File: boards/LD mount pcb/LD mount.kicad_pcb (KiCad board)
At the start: 2 copper layers, 11 x 11 mm, 5 parts

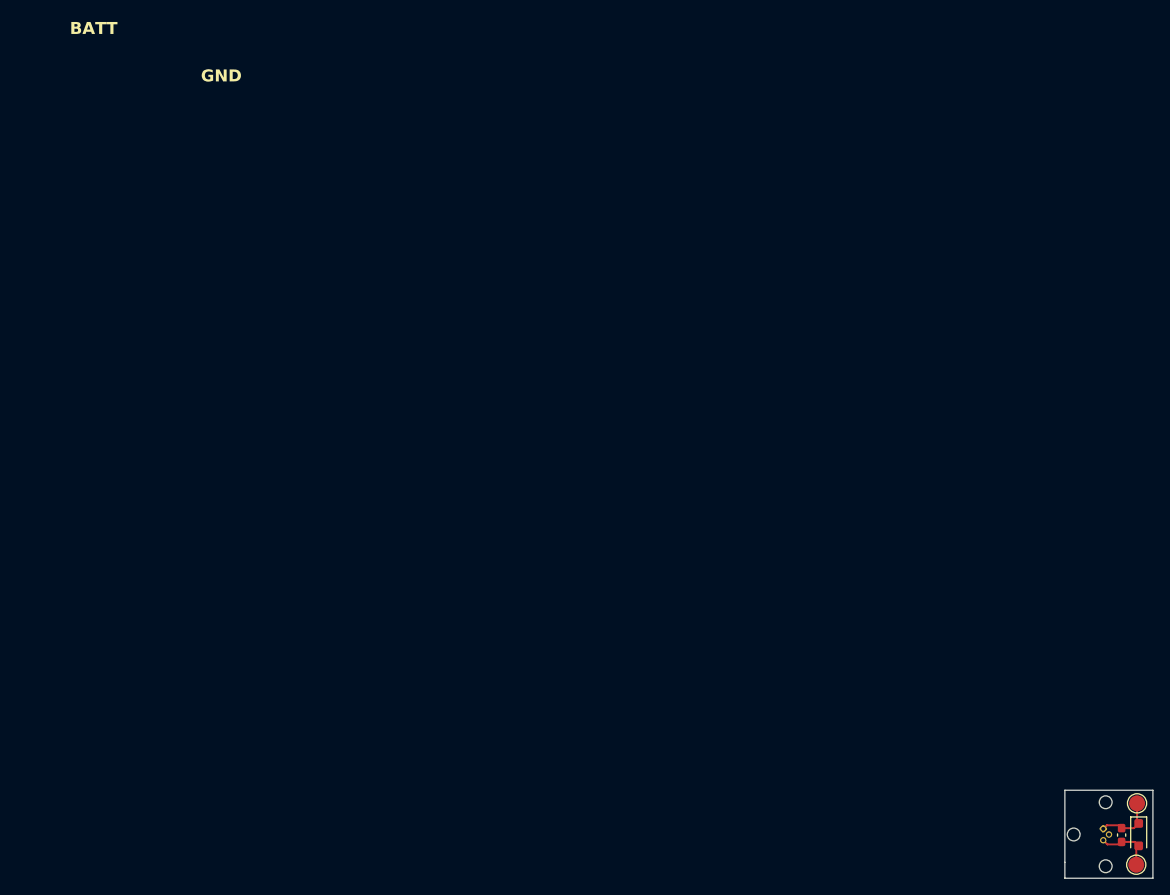
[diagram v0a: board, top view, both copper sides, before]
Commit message: updated physical scanning chassis
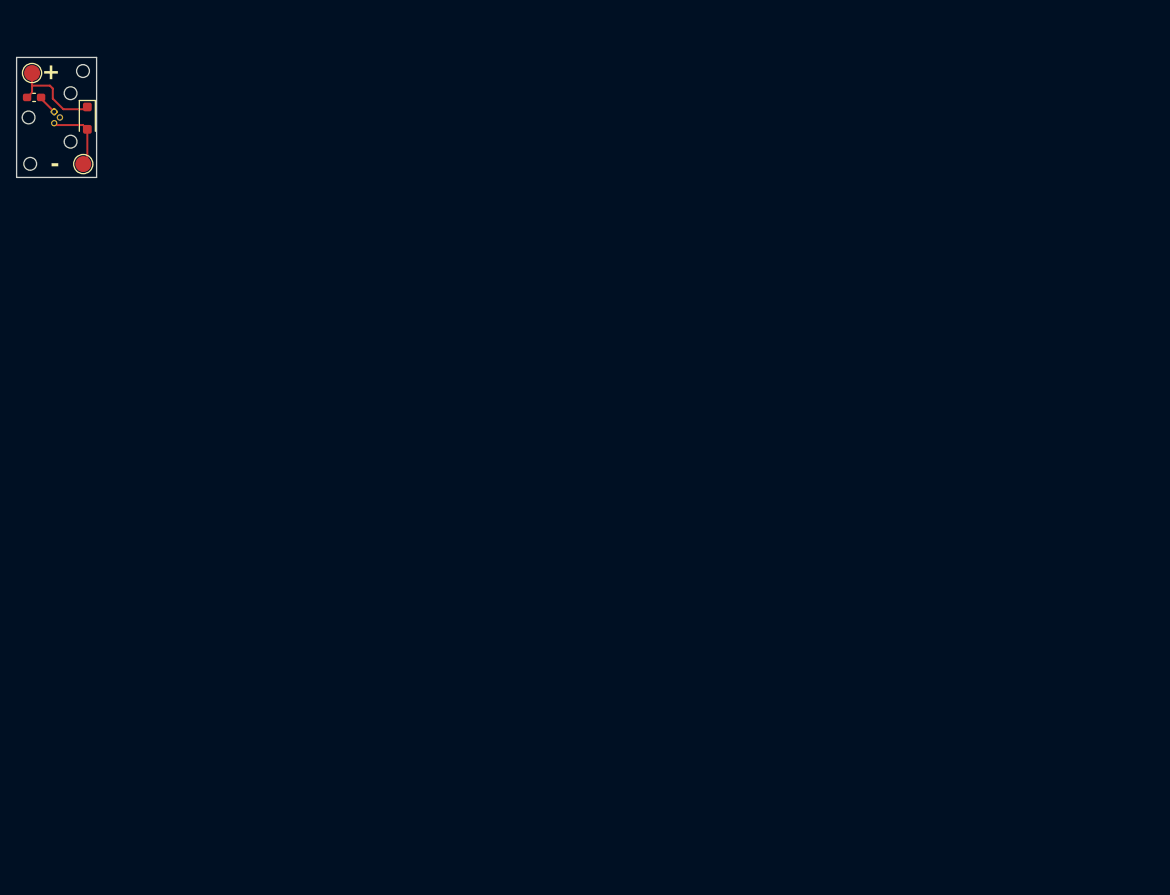
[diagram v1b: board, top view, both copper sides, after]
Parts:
- removed C1: C_Small, Capacitor_SMD:C_0603_1608Metric_Pad1.08x0.95mm_HandSolder
- added FB1: FerriteBead, Inductor_SMD:L_0603_1608Metric_Pad1.05x0.95mm_HandSolder, F.Cu at (-2.81, -2.50)
- moved TP1 165.6 mm to (-3.07, -5.55)
- moved D1 159.0 mm to (3.84, 0.09)
- moved LD1 158.4 mm to (0.00, 0.00)
- moved TP2 158.1 mm to (3.33, 5.83)
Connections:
- LD1 pad 1: Net-(D1-K) -> Net-(LD1-A)
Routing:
- net Net-(D1-K): track 7.60 -> 12.3 mm
- net Net-(LD1-A): track 0.00 -> 2.47 mm
- net Net-(D1-A): track 7.45 -> 9.01 mm
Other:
- board size 11 x 11 mm -> 10 x 15 mm
- board text added: "+"
- board text added: "-"
- board text removed: "BATT"
- board text removed: "GND"
